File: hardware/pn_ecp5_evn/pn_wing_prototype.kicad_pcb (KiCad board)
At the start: 4 copper layers, 129.5 x 52.2 mm, 261 parts, among them J101 Screw_Terminal_01x02, J102 Conn_Coaxial, J103 Conn_02x20_Odd_Even, J104 Conn_Coaxial, J105 Conn_Coaxial, J106 Conn_Coaxial, J107 Conn_01x10, J201 Conn_Coaxial, J301 Conn_Coaxial, J401 Conn_Coaxial, J601 Conn_Coaxial, J701 Conn_Coaxial, J702 Conn_Coaxial, J703 Conn_Coaxial, U201 VEMI65AB-HCI, U202 LMX2594, U301 PAT1220-C-3DB, U302 TRF37A73, U303 PAT1220-C-3DB, U401 PAT1220-C-3DB, U402 TRF37A73, U403 PAT1220-C-3DB, U501 LM27761, U502 ADM7171ACPZ-3.3-R7, U503 TPS72301DB, U601 LM2904, U602 OPA2211, U701 SYM-63LH+, U702 ADG621, U703 OPA2211, U801 THS4551, U802 LT6657BHMS8-2.5, U901 ADS7868, U902 ADS7868, U903 Si8640BB-B-IU, U904 Si8640BB-B-IU, U905 Si8642BB-B-IU, X601 ABLNO

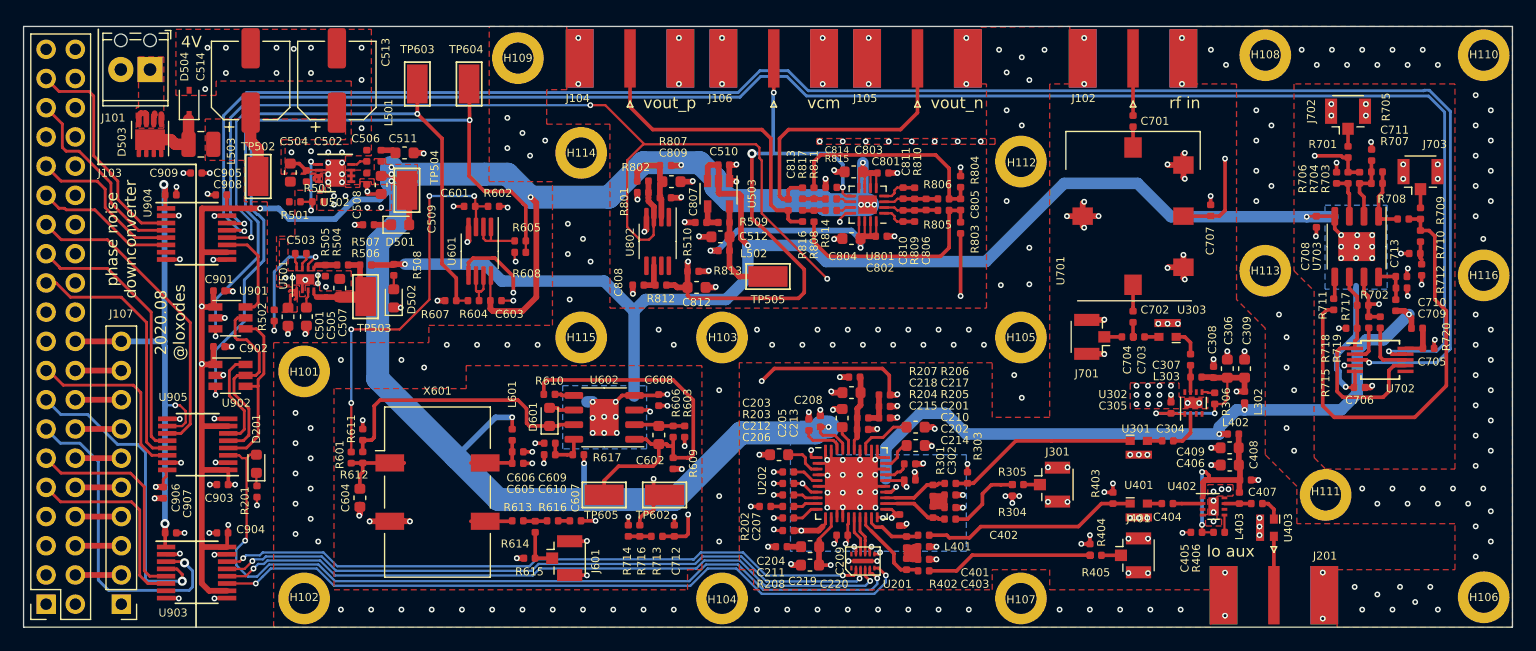
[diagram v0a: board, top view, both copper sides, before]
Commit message: added bottom layer ground plane, via cleanup
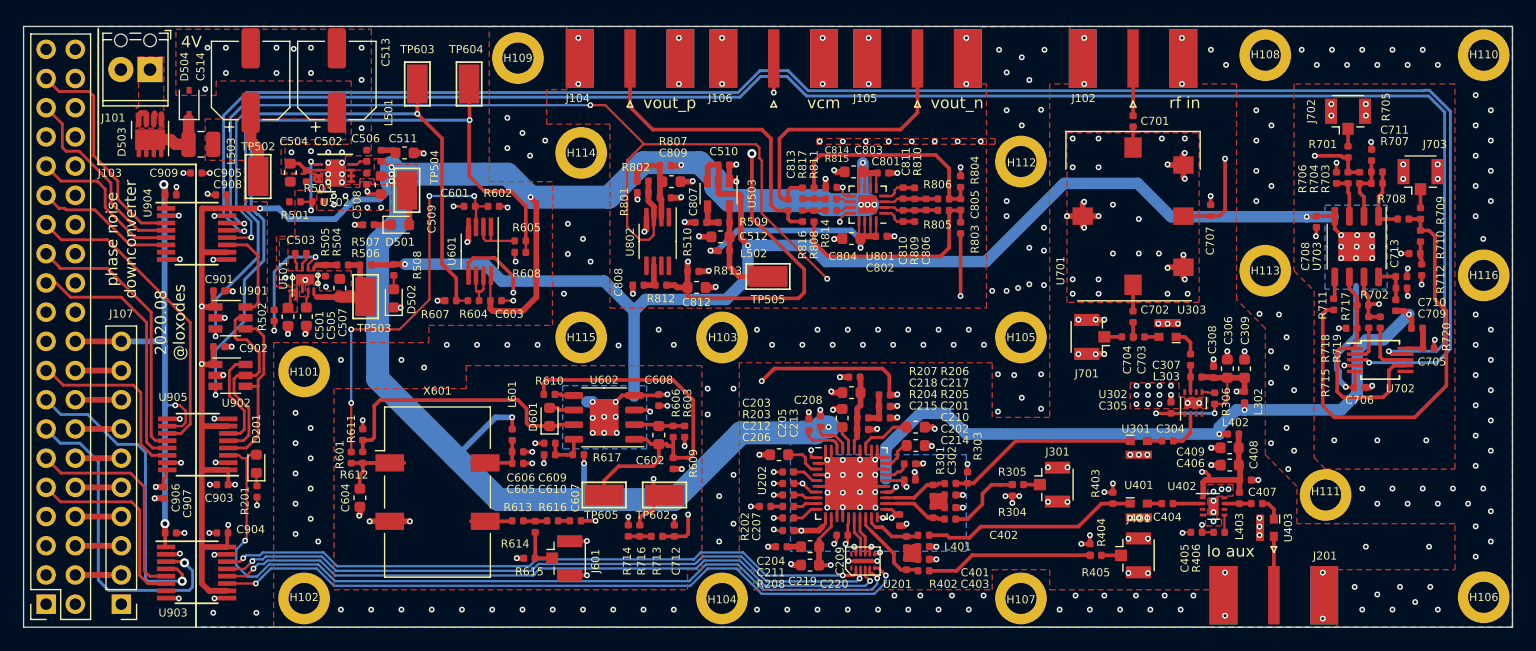
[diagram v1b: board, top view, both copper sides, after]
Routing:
- net GND: vias 398 -> 456
- added copper zone on B.Cu, net GND

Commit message: drc and erc check, schematic cleanup
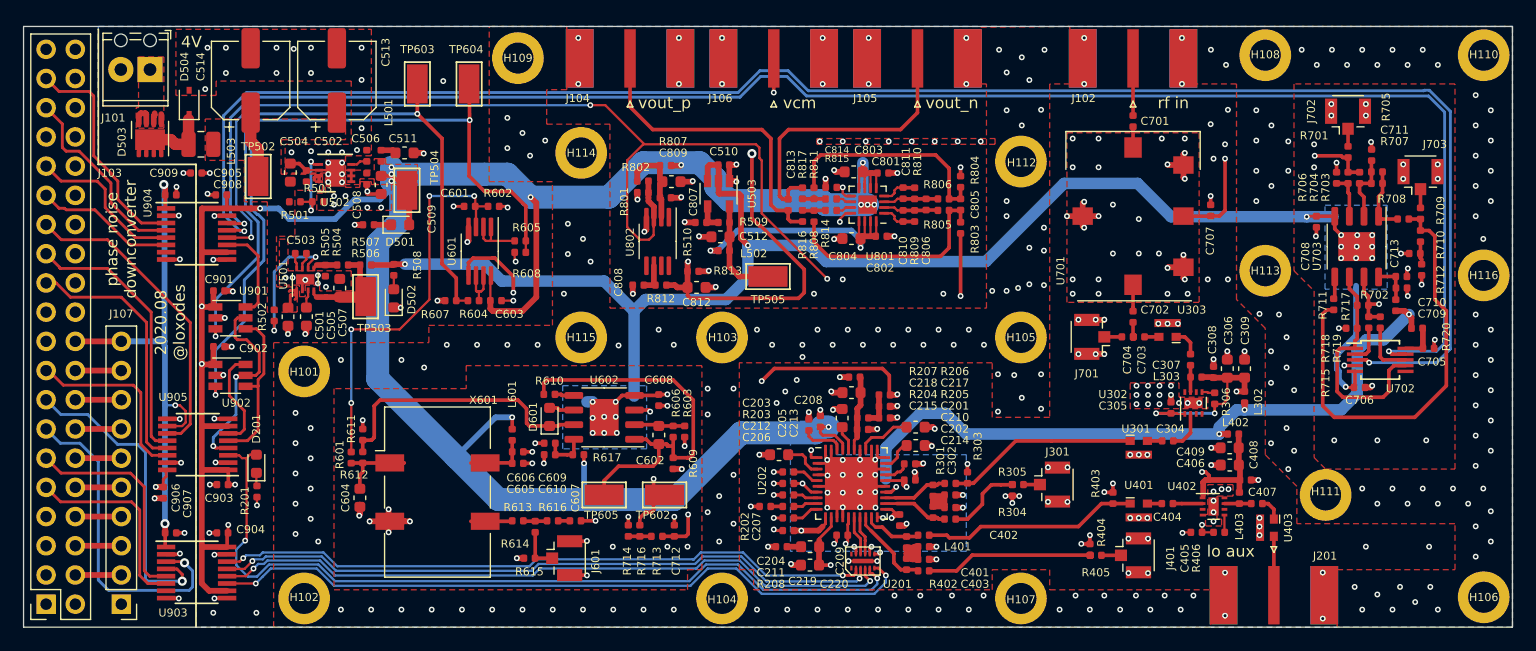
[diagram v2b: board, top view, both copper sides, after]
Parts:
- removed G***: LOGO, vna:cat
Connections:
- J103 pad 23: /isolator/ADC_SCK -> /isolator/ADC_SDO
- J103 pad 25: /isolator/ADC_SDO -> /isolator/ADC_SCK
- U905 pad 12: /isolator/ADC_SDO -> /isolator/ADC_SCK
- U905 pad 13: /isolator/ADC_SCK -> /isolator/ADC_SDO
- U905 pad 4: /isolator/ADC_SCK_ISO -> /isolator/ADC_SDO_ISO
- U905 pad 5: /isolator/ADC_SDO_ISO -> /isolator/ADC_SCK_ISO
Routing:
- net GND: track 156.7 -> 160.9 mm, vias 456 -> 482
- net Net-(U201-Pad11): track 13.8 -> 12.6 mm
- net /synth/REF_IN: track 20.7 -> 19.5 mm
- net /isolator/ADC_SDO: track 23.6 -> 22.6 mm
- net /isolator/ADC_SCK: track 22.6 -> 23.6 mm
- net /isolator/ADC_SCK_ISO: track 15.1 -> 14.3 mm
- net /isolator/ADC_SDO_ISO: track 16.7 -> 17.2 mm, vias 0 -> 2

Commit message: checked stability of LO amplifier, started migen project, added more flexibility for active filtering on baseband path
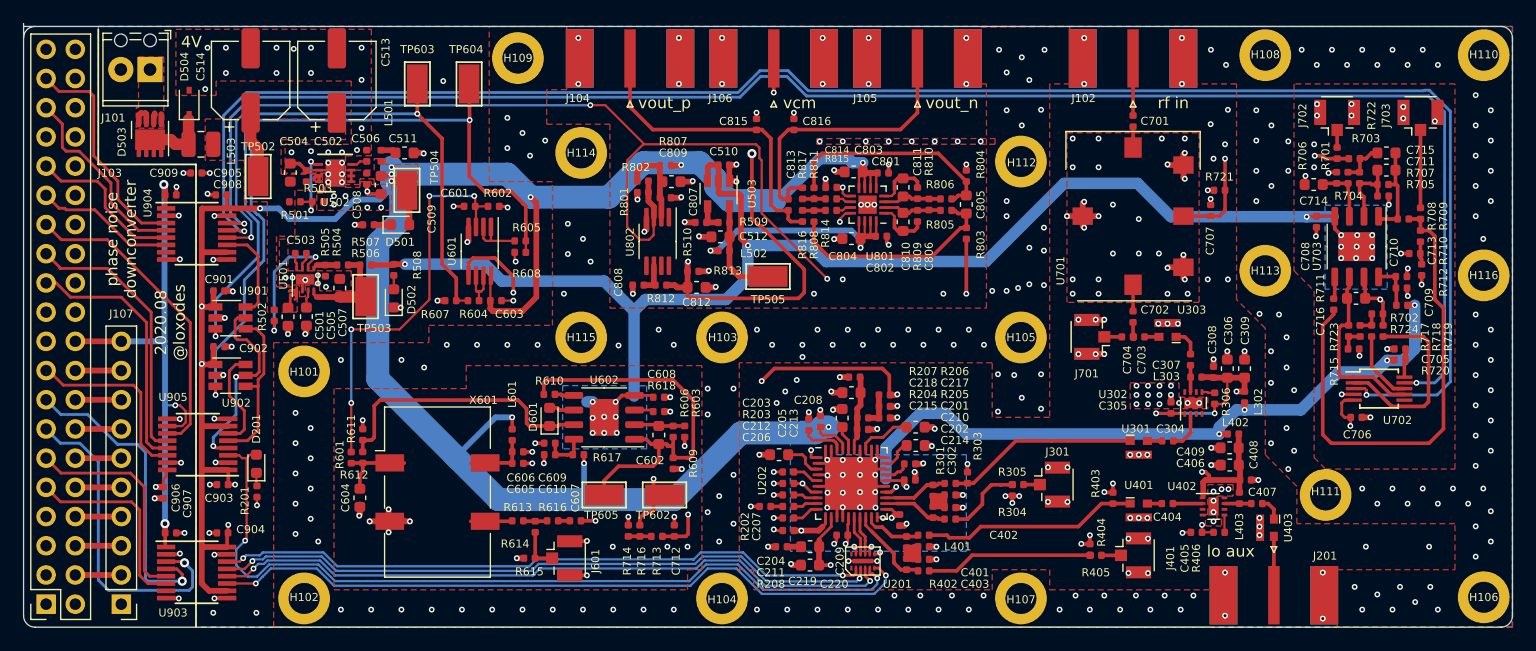
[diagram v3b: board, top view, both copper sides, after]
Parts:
- added C714: DNI, Capacitor_SMD:C_0603_1608Metric, F.Cu at (142.2, 79.5)
- added C715: DNI, Capacitor_SMD:C_0603_1608Metric, F.Cu at (148.5, 76.8)
- added C716: DNI, Capacitor_SMD:C_0603_1608Metric, F.Cu at (145.9, 89.4)
- added C815: DNI, Capacitor_SMD:C_0402_1005Metric, F.Cu at (93.8, 74.3)
- added C816: DNI, Capacitor_SMD:C_0402_1005Metric, F.Cu at (97.0, 74.3)
- added R618: 51, Resistor_SMD:R_0402_1005Metric, F.Cu at (85.2, 99.2)
- added R721: 50, Resistor_SMD:R_0402_1005Metric, F.Cu at (134.0, 80.0)
- added R722: 0, Resistor_SMD:R_0402_1005Metric, F.Cu at (145.8, 77.2)
- added R723: DNI, Resistor_SMD:R_0402_1005Metric, F.Cu at (145.2, 92.2)
- added R724: 10k, Resistor_SMD:R_0402_1005Metric, F.Cu at (147.8, 90.8)
- C602, C610, C710: value C_Small -> 1 uF
- C608, C609, C708, C709: value C_Small -> 10 nF
- C702: value DNI -> 1 nF
- C711: footprint Capacitor_SMD:C_0402_1005Metric -> Capacitor_SMD:C_0603_1608Metric
- C805: value C_Small -> 470 pF; footprint Capacitor_SMD:C_0402_1005Metric -> Capacitor_SMD:C_0603_1608Metric
- C806: value C_Small -> 1 nF
- C810, C811: value C_Small -> 270 pF; footprint Capacitor_SMD:C_0402_1005Metric -> Capacitor_SMD:C_0603_1608Metric
- C813: value C_Small -> 22 nF
- R603: value R_Small -> 51
- R606: value R_Small -> 220k
- R609: value R_Small -> 51k
- R617, R702, R720: value R_Small -> BLM15GG471
- R704, R706, R709, R714, R809, R810: value R_Small -> DNI
- R708, R710, R711: value R_Small -> 17
- R712, R713, R716, R717, R718: value R_Small -> 0
- R715: value R_Small -> 100
- R719: value R_Small -> 1k
- R803, R804: value R_Small -> 1.2k
- R805, R806: value R_Small -> 330
- R814, R815: value R_Small -> 5
- R816, R817: value R_Small -> 10
- moved J703 5.15 mm to (151.5, 73.7)
- moved R705 3.70 mm to (148.2, 80.5), turned to 0 degrees
- moved R720 3.13 mm to (149.7, 94.8)
- moved C706 2.62 mm to (145.9, 99.8)
- moved U702 2.50 mm to (147.9, 97.2)
- moved C705 2.49 mm to (149.7, 93.8), turned to 0 degrees
- moved R717 2.25 mm to (146.2, 92.2), turned to 270 degrees
- moved R715 1.81 mm to (145.7, 93.8), turned to 0 degrees
- moved R719 1.46 mm to (148.2, 92.2)
- moved R718 1.06 mm to (147.2, 92.2)
- moved J702 0.96 mm to (144.2, 73.7)
- moved R701 0.96 mm to (144.2, 76.8)
- moved C711 0.84 mm to (148.5, 78.2)
- moved R804 0.71 mm to (112.0, 78.8)
- moved R803 0.70 mm to (112.0, 83.8)
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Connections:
- R703 pad 2: Net-(C707-Pad2) -> Net-(C715-Pad2)
- R704 pad 1: Net-(C707-Pad2) -> Net-(C715-Pad2)
- R717 pad 1: /adc/ADC_VIN -> Net-(R717-Pad1)
- R718 pad 1: /adc/ADC_VIN -> Net-(R717-Pad1)
- U602 pad 3: GND -> Net-(R618-Pad2)
- U702 pad 1: Net-(R715-Pad1) -> Net-(C716-Pad2)
- U702 pad 7: Net-(R715-Pad1) -> Net-(C716-Pad2)
- U703 pad 6: Net-(R715-Pad1) -> Net-(C716-Pad2)
- U801 pad 17: +3V3 -> GND
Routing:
- net -3V3: track 135.1 -> 154.2 mm, vias 22 -> 21
- net Net-(R715-Pad1): track 20.1 -> 2.10 mm
- net Net-(C716-Pad2): track 0.00 -> 15.9 mm
- net Net-(R719-Pad2): track 3.33 -> 16.9 mm
- net Net-(J703-Pad1): track 1.63 -> 6.78 mm
- net Net-(R708-Pad1): track 38.3 -> 43.1 mm
- net Net-(C715-Pad2): track 0.00 -> 3.92 mm
- net /IF_G2: track 152.1 -> 155.4 mm
- net +3V3: track 312.3 -> 309.0 mm, vias 27 -> 25
- net Net-(C711-Pad1): track 5.96 -> 8.39 mm
- net Net-(R717-Pad1): track 0.00 -> 2.01 mm
- net Net-(C707-Pad2): track 21.5 -> 19.5 mm
- net Net-(R618-Pad2): track 0.00 -> 1.68 mm
- net Net-(R718-Pad2): track 4.83 -> 6.41 mm
- net Net-(C810-Pad1): track 3.37 -> 4.77 mm
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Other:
- board size 129.5 x 52.2 mm -> 129.5 x 52.5 mm

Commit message: final layout cleanup, ordered phase noise downconverter boards
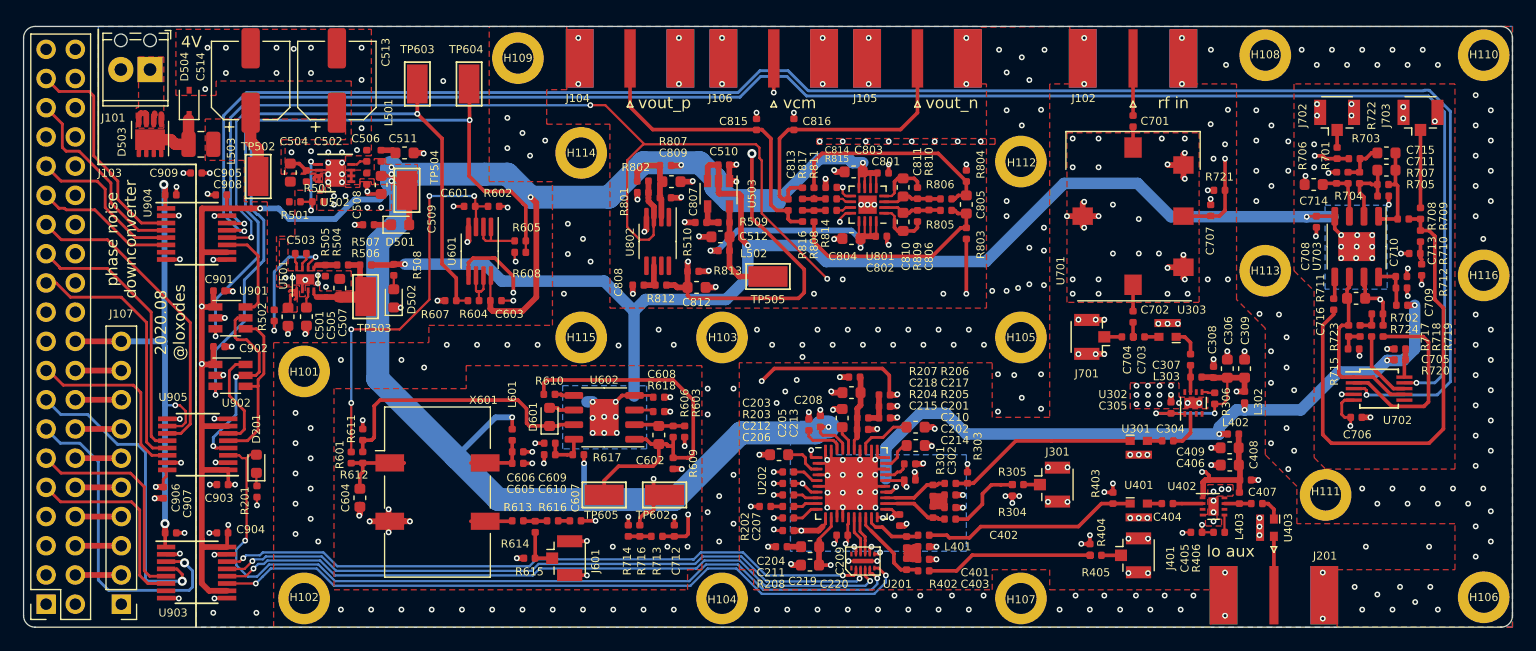
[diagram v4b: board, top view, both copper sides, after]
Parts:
- added G***: LOGO, vna:cat, B.Cu at (68.5, 103.5)
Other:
- board size 129.5 x 52.5 mm -> 129.5 x 52.2 mm

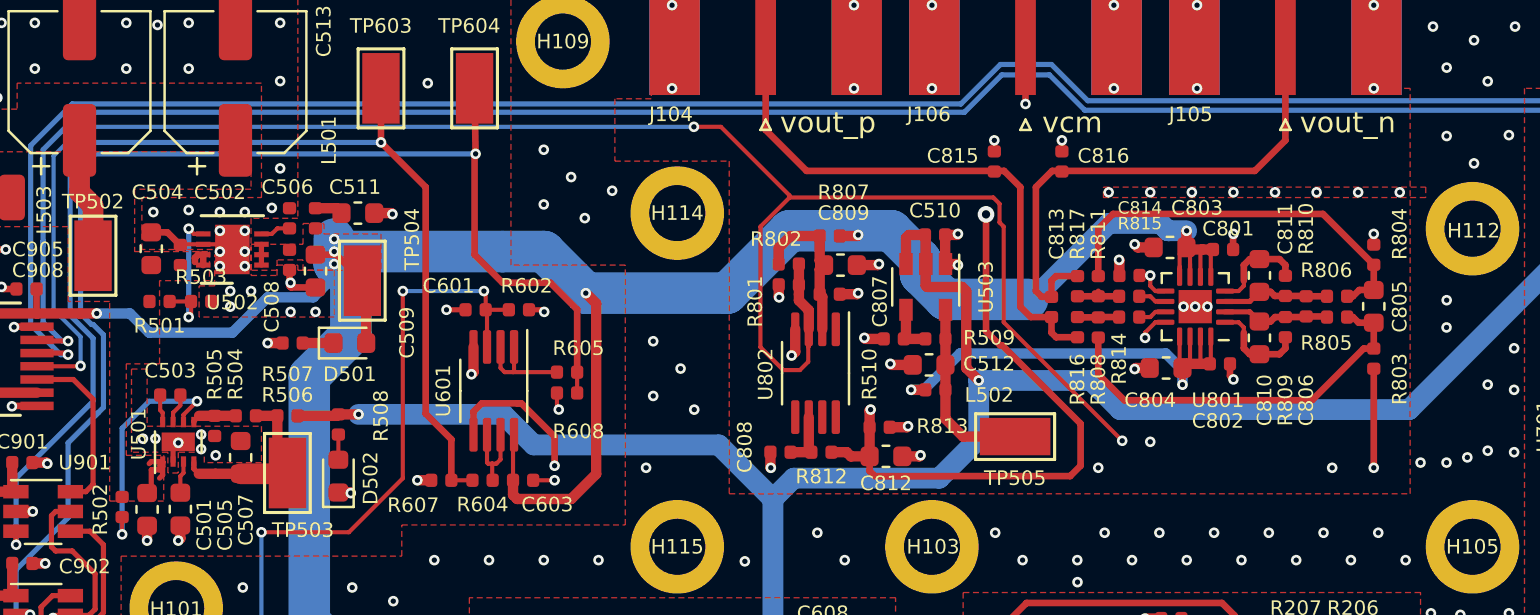
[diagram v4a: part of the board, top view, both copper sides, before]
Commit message: added part numbers to schematic of phase noise downconverter, ordered
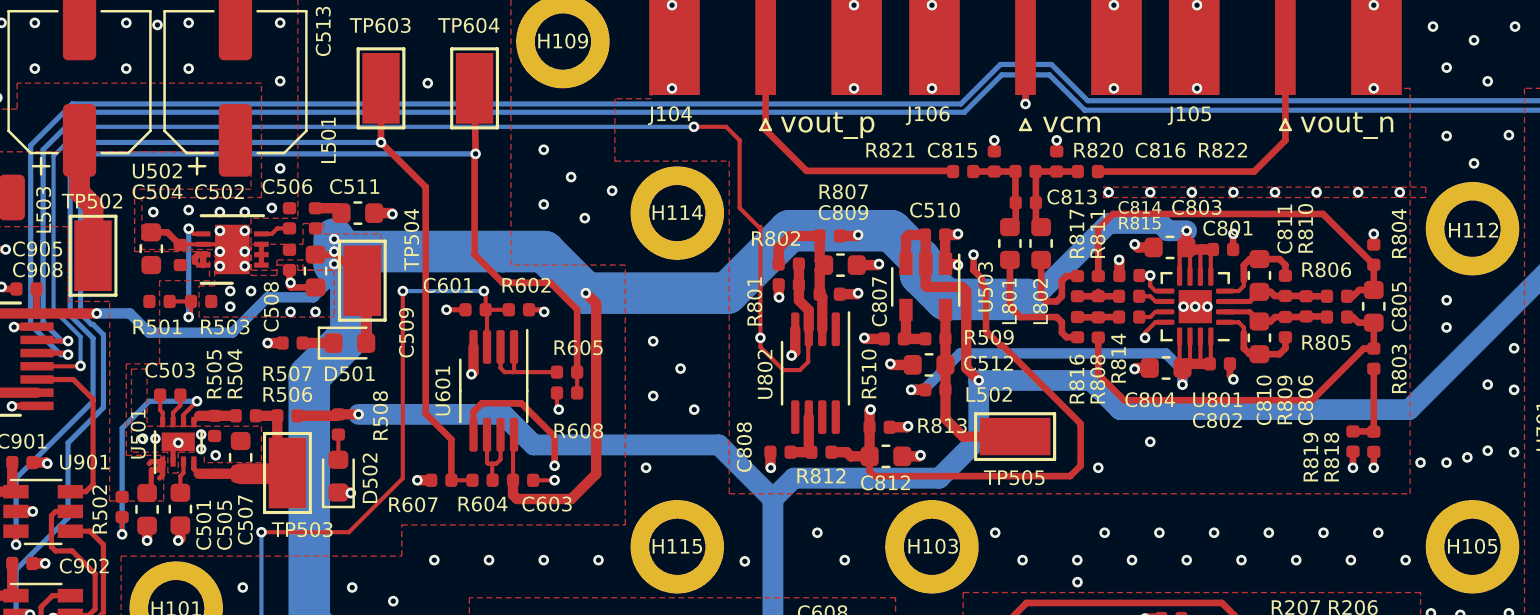
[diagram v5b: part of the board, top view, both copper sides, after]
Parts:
- removed G***: LOGO, vna:cat
- added L801: 390 nH, Inductor_SMD:L_0603_1608Metric, F.Cu at (94.5, 78.2)
- added L802: 390 nH, Inductor_SMD:L_0603_1608Metric, F.Cu at (96.0, 78.2)
- added R818: 1.2k, Resistor_SMD:R_0402_1005Metric, F.Cu at (112.0, 87.8)
- added R819: 1.2k, Resistor_SMD:R_0402_1005Metric, F.Cu at (111.0, 87.7)
- added R820: 732, Resistor_SMD:R_0402_1005Metric, F.Cu at (95.2, 74.8)
- added R821: 5.6, Resistor_SMD:R_0402_1005Metric, F.Cu at (92.2, 74.8)
- added R822: 5.6, Resistor_SMD:R_0402_1005Metric, F.Cu at (98.2, 74.8)
- C607: value C_Small -> 10 nF
- C711, C716: value DNI -> 10 pF
- C813: value 22 nF -> 360 pF
- R613, R713, R716: value 0 -> 100
- R614, R615: value DNI -> 100
- R701: value R_Small -> 0
- R703: value R_Small -> DNI
- R704: value DNI -> 0
- R705: value R_Small -> 1k
- R707: value R_Small -> 4.7k
- R714: value DNI -> 1.7k
- R808, R811: value R_Small -> 1.2k
- R814, R815: value 5 -> 0
- R816, R817: value 10 -> 40.2
- moved C813 5.16 mm to (95.3, 76.2), turned to 0 degrees
- moved C816 0.25 mm to (96.8, 74.3)
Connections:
- C813 pad 1: /adc/VOUT_P -> Net-(C813-Pad1)
- C813 pad 2: /adc/VOUT_N -> Net-(C813-Pad2)
- C815 pad 2: /adc/VOUT_P -> Net-(C813-Pad1)
- C816 pad 1: /adc/VOUT_N -> Net-(C813-Pad2)
- R803 pad 2: /adc/ADC_VIN -> Net-(R803-Pad2)
- R816 pad 1: /adc/VOUT_P -> Net-(L801-Pad1)
- R817 pad 1: /adc/VOUT_N -> Net-(L802-Pad1)
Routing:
- net /adc/VOUT_P: track 27.2 -> 14.1 mm
- net /adc/VOUT_N: track 25.6 -> 14.4 mm
- net /BUF_~PD: track 97.2 -> 87.2 mm
- net Net-(L801-Pad1): track 0.00 -> 6.40 mm
- net Net-(C813-Pad1): track 0.00 -> 4.83 mm
- net Net-(C813-Pad2): track 0.00 -> 4.81 mm
- net Net-(L802-Pad1): track 0.00 -> 4.55 mm
- net Net-(R803-Pad2): track 0.00 -> 4.04 mm
- net /adc/ADC_VIN: track 46.9 -> 42.9 mm
- net GND: track 161.7 -> 162.5 mm
